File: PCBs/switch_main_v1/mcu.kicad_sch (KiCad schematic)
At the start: 1 part, among them U301 STM32H573RIVx

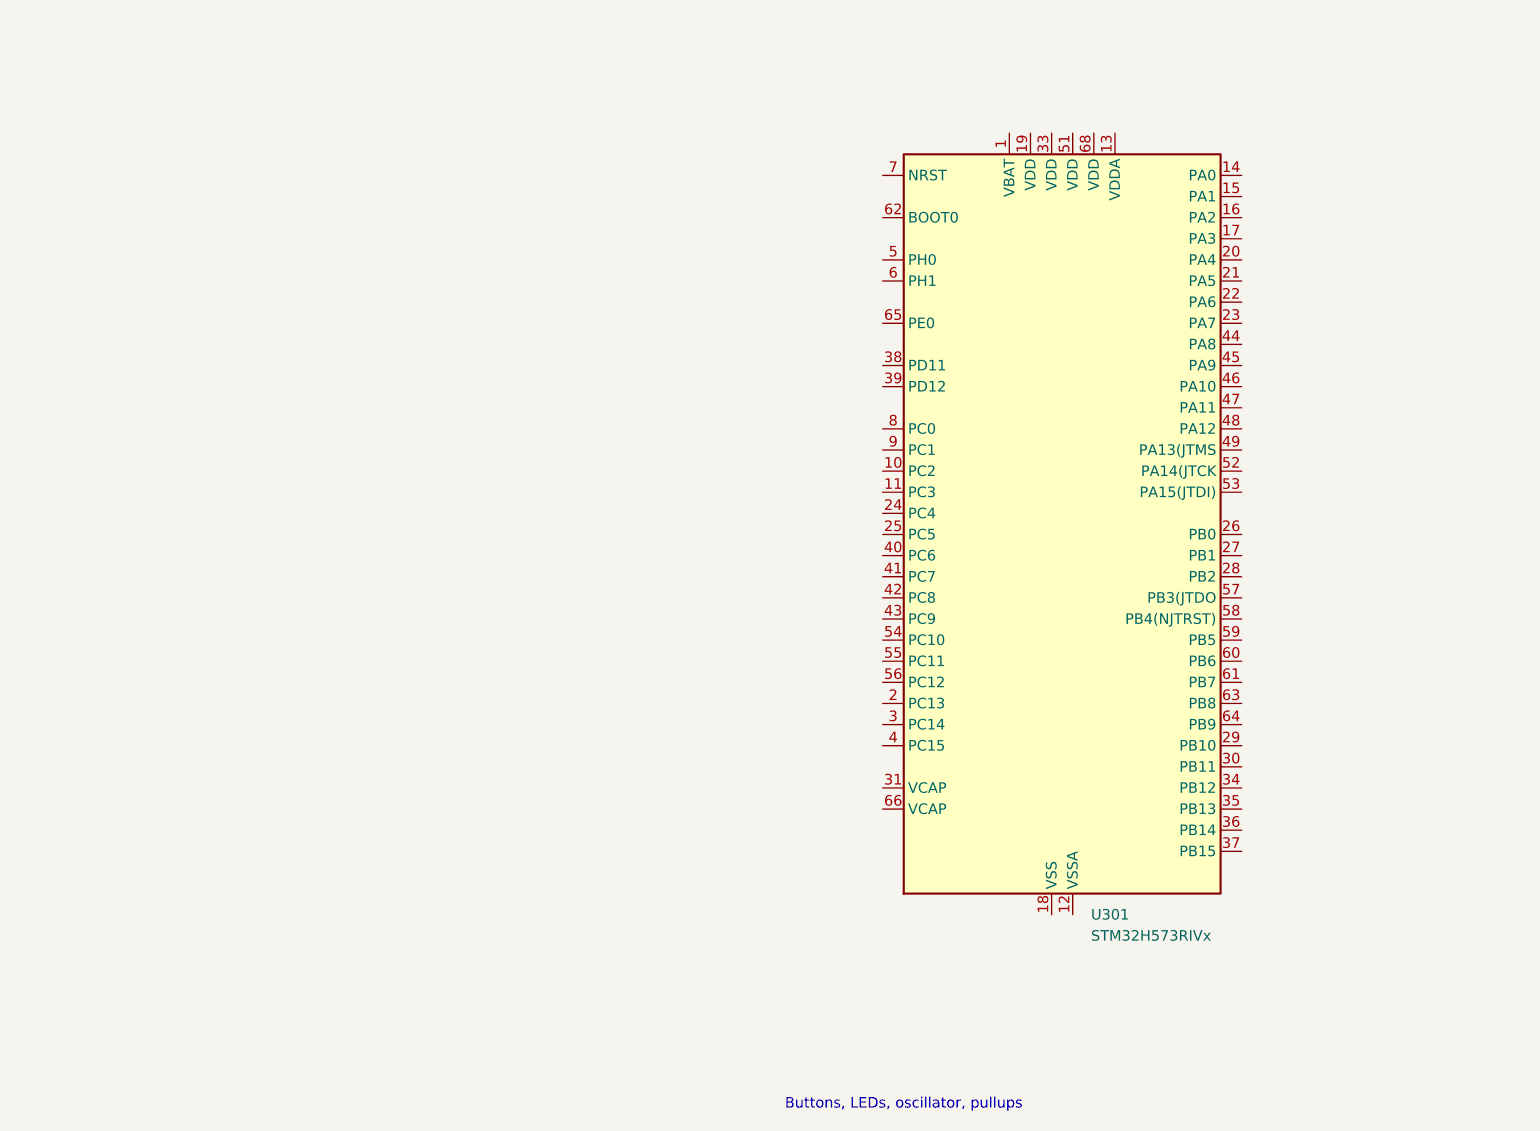
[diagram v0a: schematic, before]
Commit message: Connectors schematic almost complete
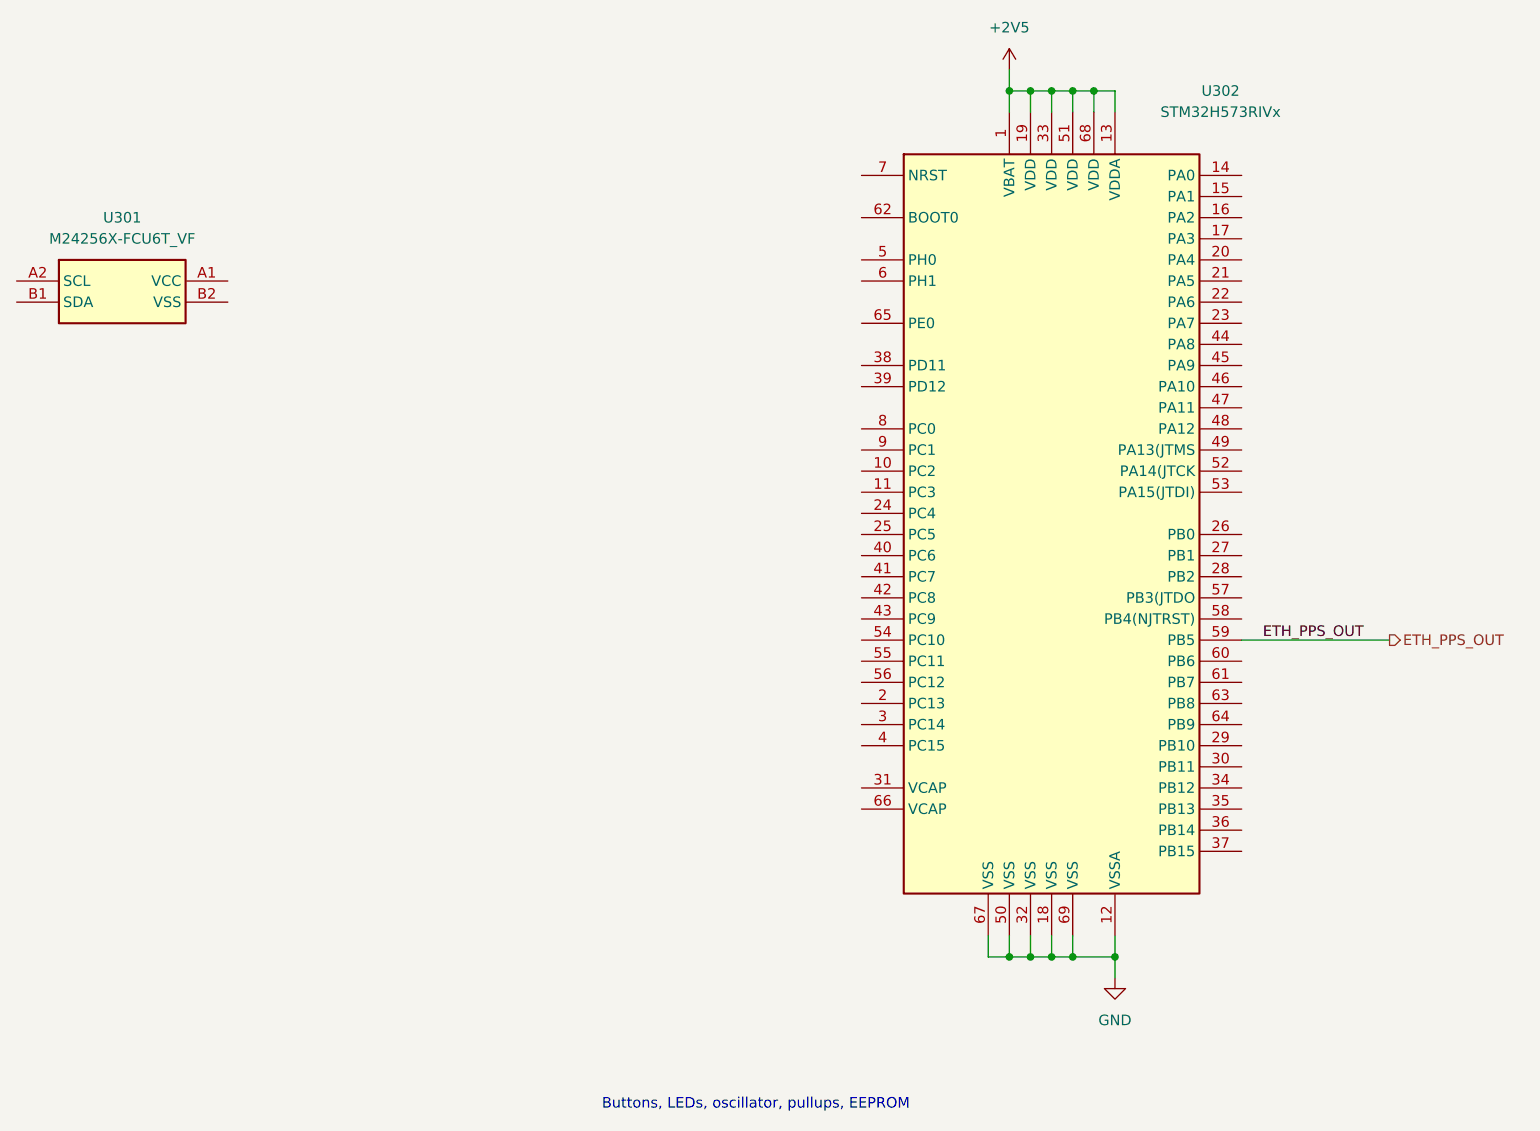
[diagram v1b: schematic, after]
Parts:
- added U301: M24256X-FCU6T_VF, switch_footprints:BGA4C50P2X2_70X98X33, symbol M24256X-FCU6T_VF:M24256X-FCU6T_VF
- renumbered U301 to U302
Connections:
- net +2V5: now reaches U302.1 (VBAT)
- net +2V5: now also U302.13 (VDDA), U302.19 (VDD), U302.33 (VDD), U302.51 (VDD), U302.68 (VDD)
- net GND: now reaches U302.12 (VSSA)
- net GND: now also U302.18 (VSS), U302.32 (VSS), U302.50 (VSS), U302.67 (VSS), U302.69 (VSS)
- net ETH_PPS_OUT: now reaches U302.59 (PB5)
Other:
- note added: "Buttons, LEDs, oscillator, pullups, EEPROM"
- note removed: "Buttons, LEDs, oscillator, pullups"

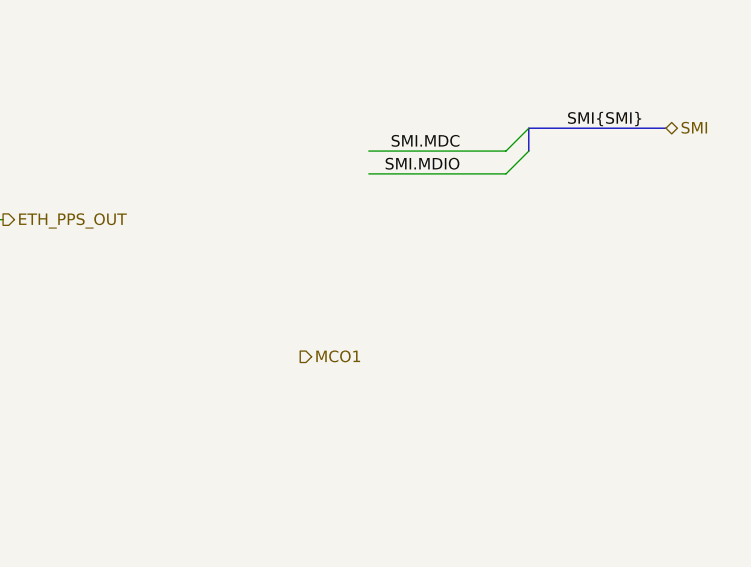
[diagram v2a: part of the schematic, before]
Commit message: Block diagram layout change
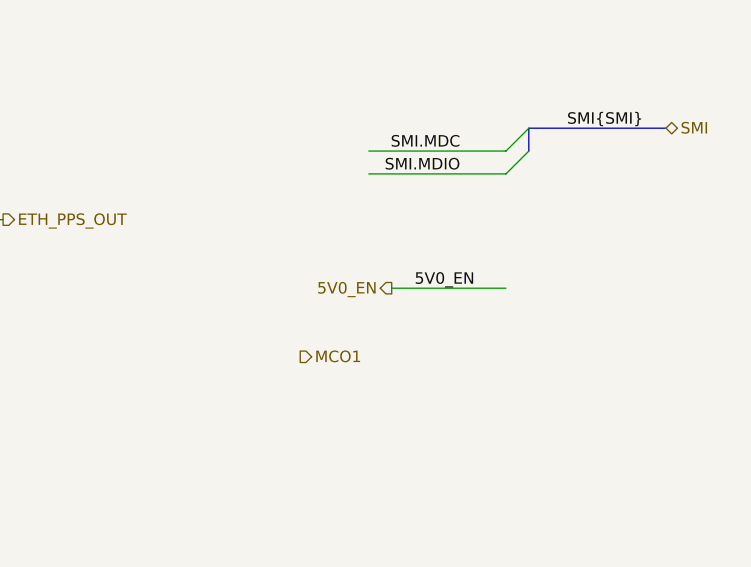
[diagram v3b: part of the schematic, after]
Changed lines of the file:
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@@
 	(generator_version "8.0")
 	(paper "A4")
+	(title_block
+		(date "2024-04-06")
+		(rev "0.0.0")
+	)

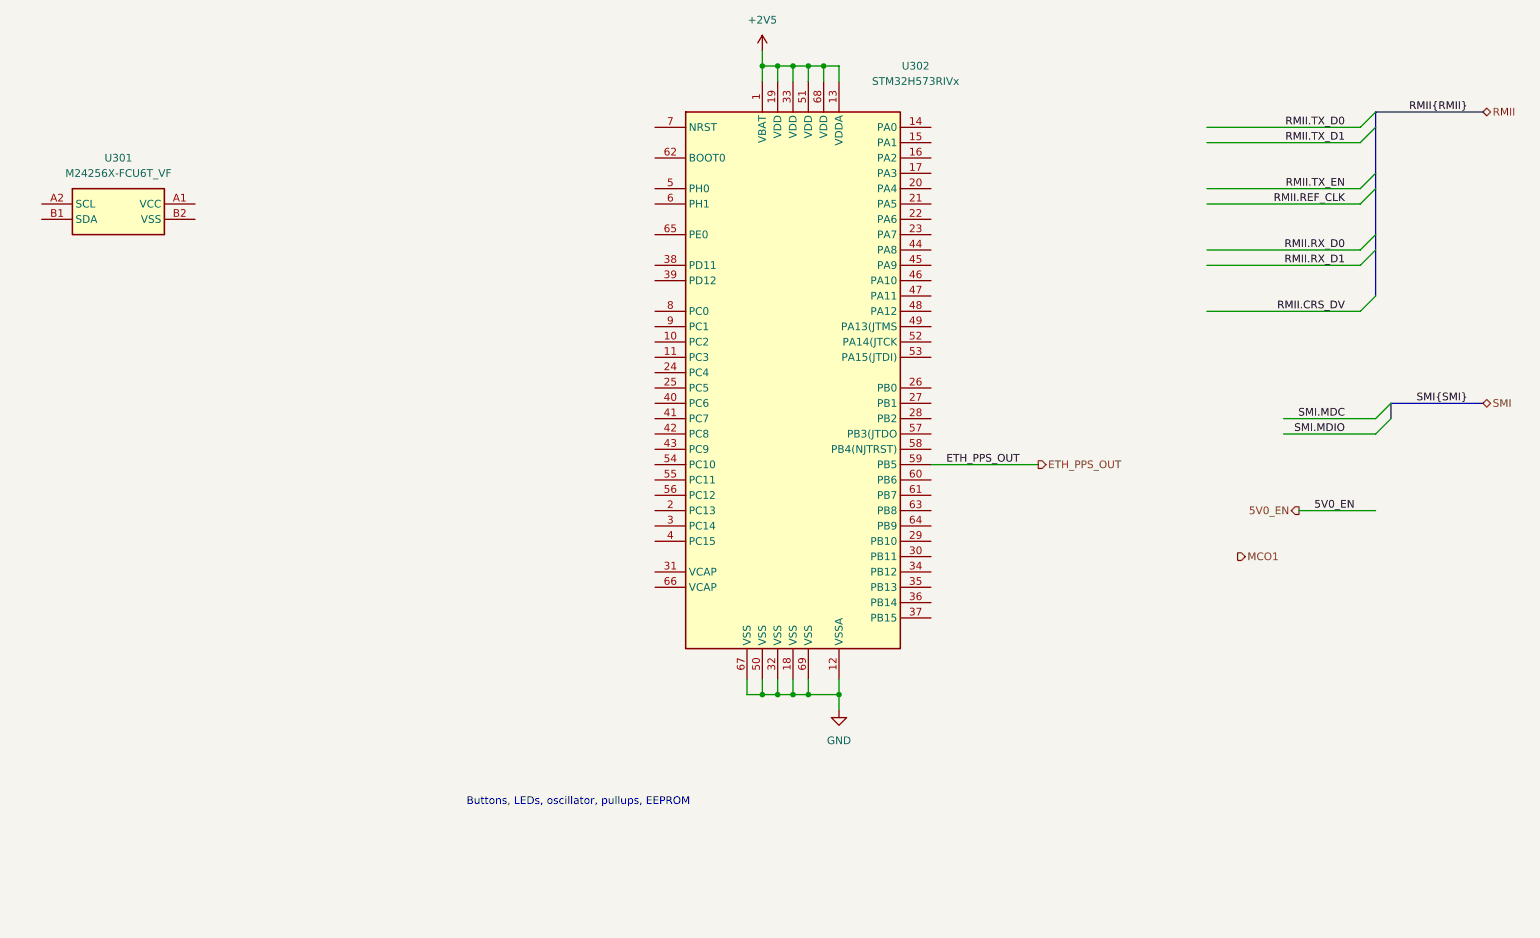
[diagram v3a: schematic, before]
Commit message: GbE part of schematic done
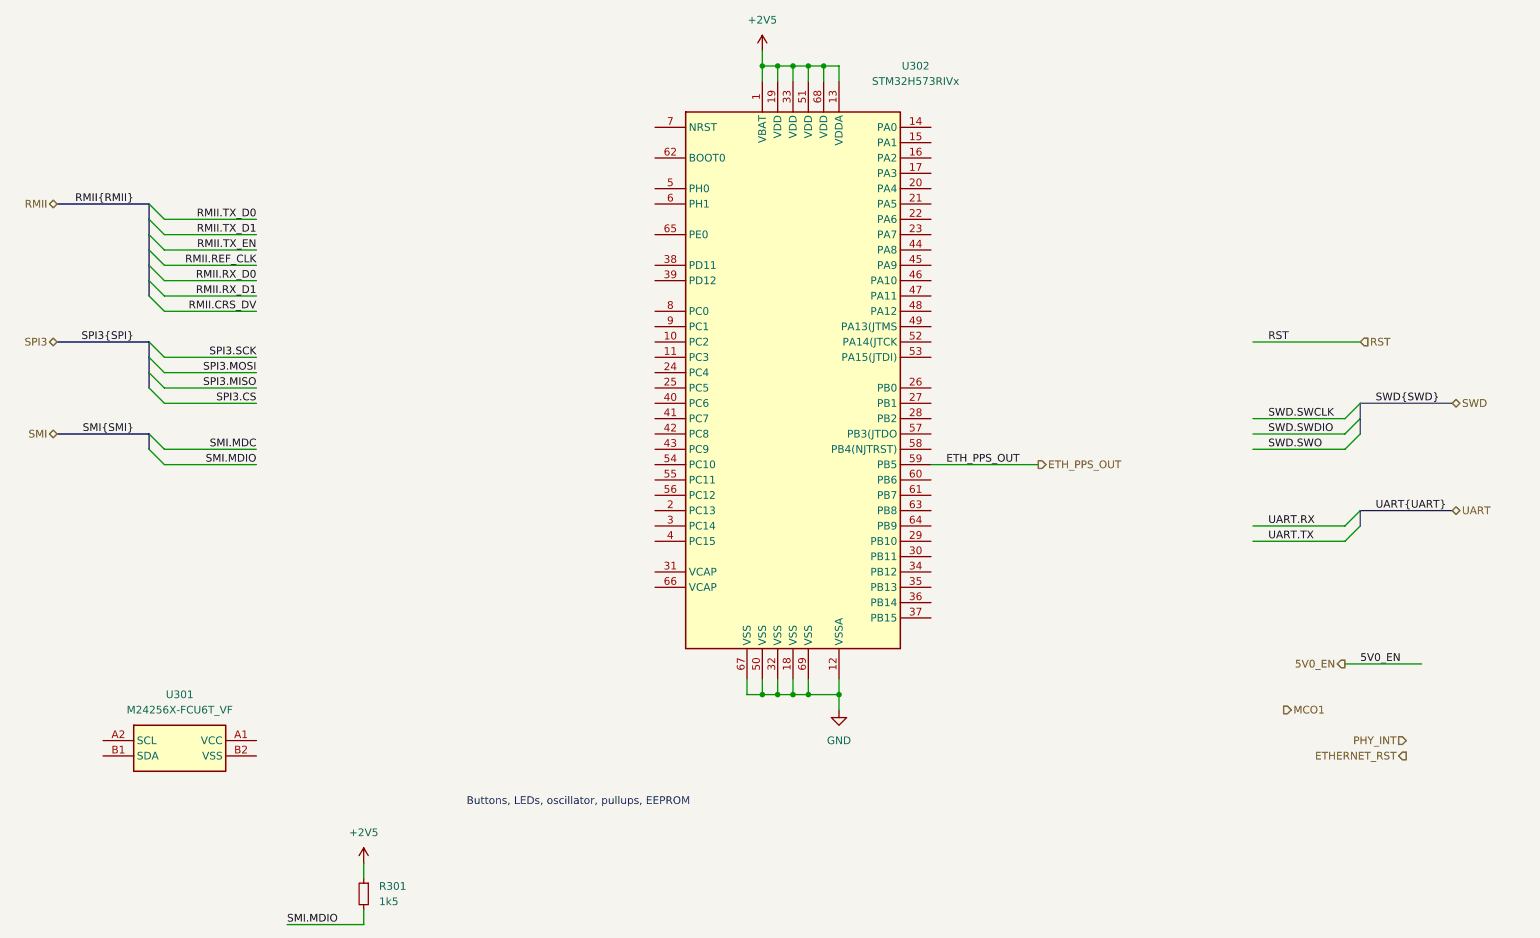
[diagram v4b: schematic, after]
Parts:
- added R301: 1k5, Resistor_SMD:R_0402_1005Metric, symbol Device:R_Small
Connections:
- net +2V5: now also R301.1
- net SMI.MDIO: now also R301.2
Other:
- company: (none) -> Ben Smith
- moved on the sheet: U301
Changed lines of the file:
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@@
 		(date "2024-04-06")
 		(rev "0.0.0")
+		(company "Ben Smith")
 	)

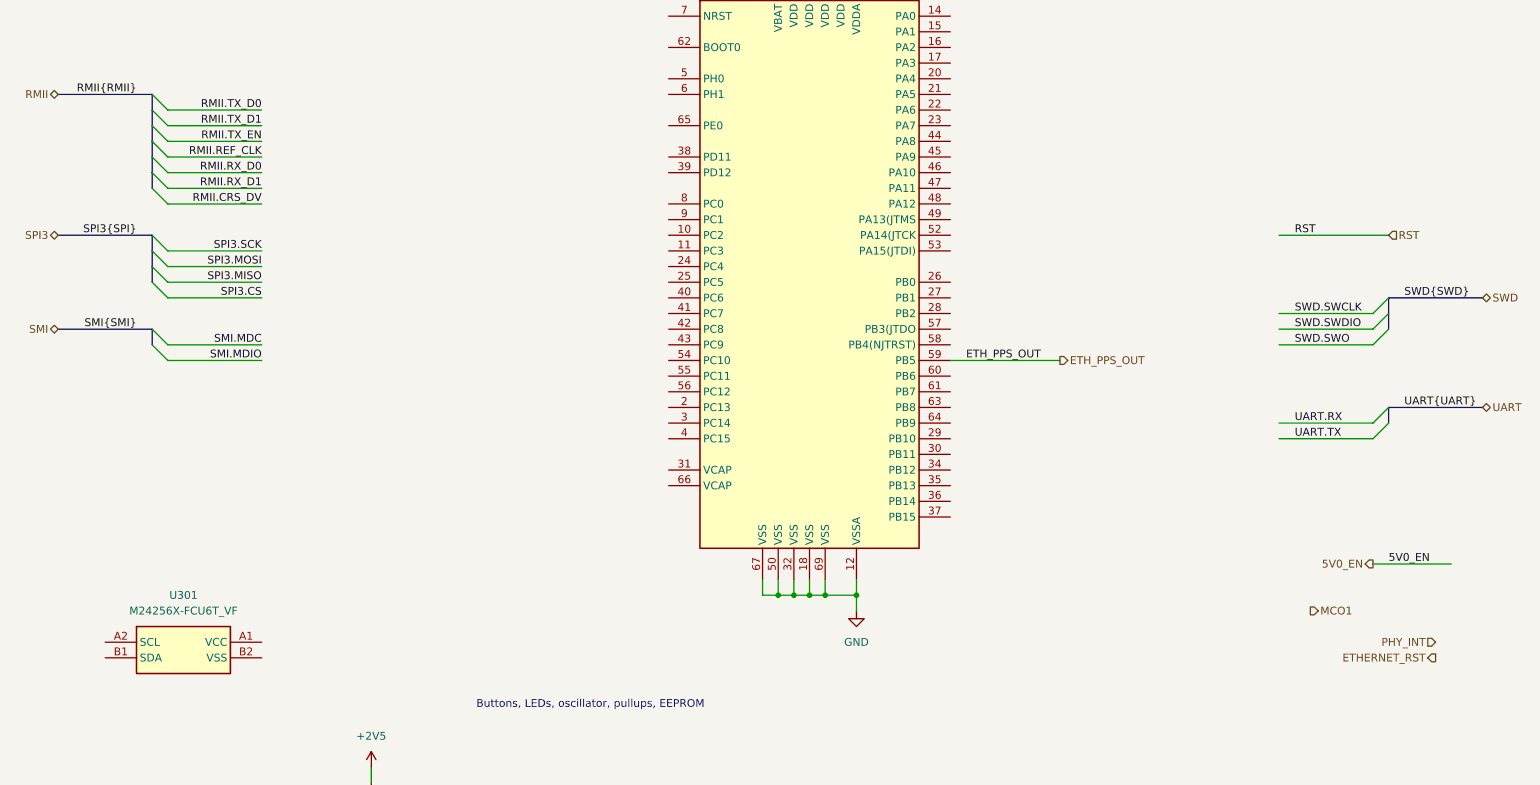
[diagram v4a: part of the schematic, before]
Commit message: Progress on CAN schematic sheet
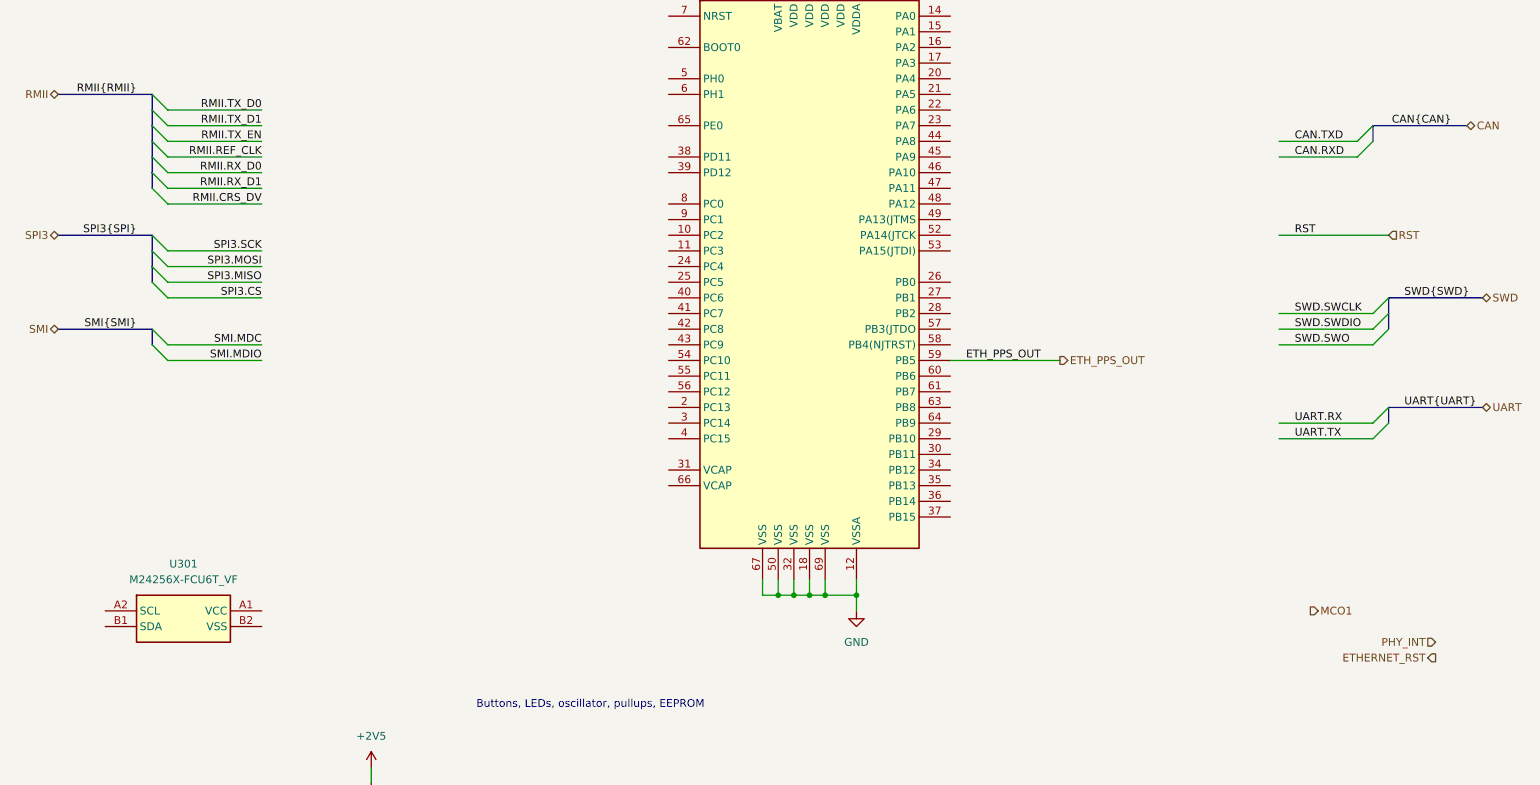
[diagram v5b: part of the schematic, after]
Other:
- moved on the sheet: U301
